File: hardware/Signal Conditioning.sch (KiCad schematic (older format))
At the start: 15 parts, among them U2 LM2902N

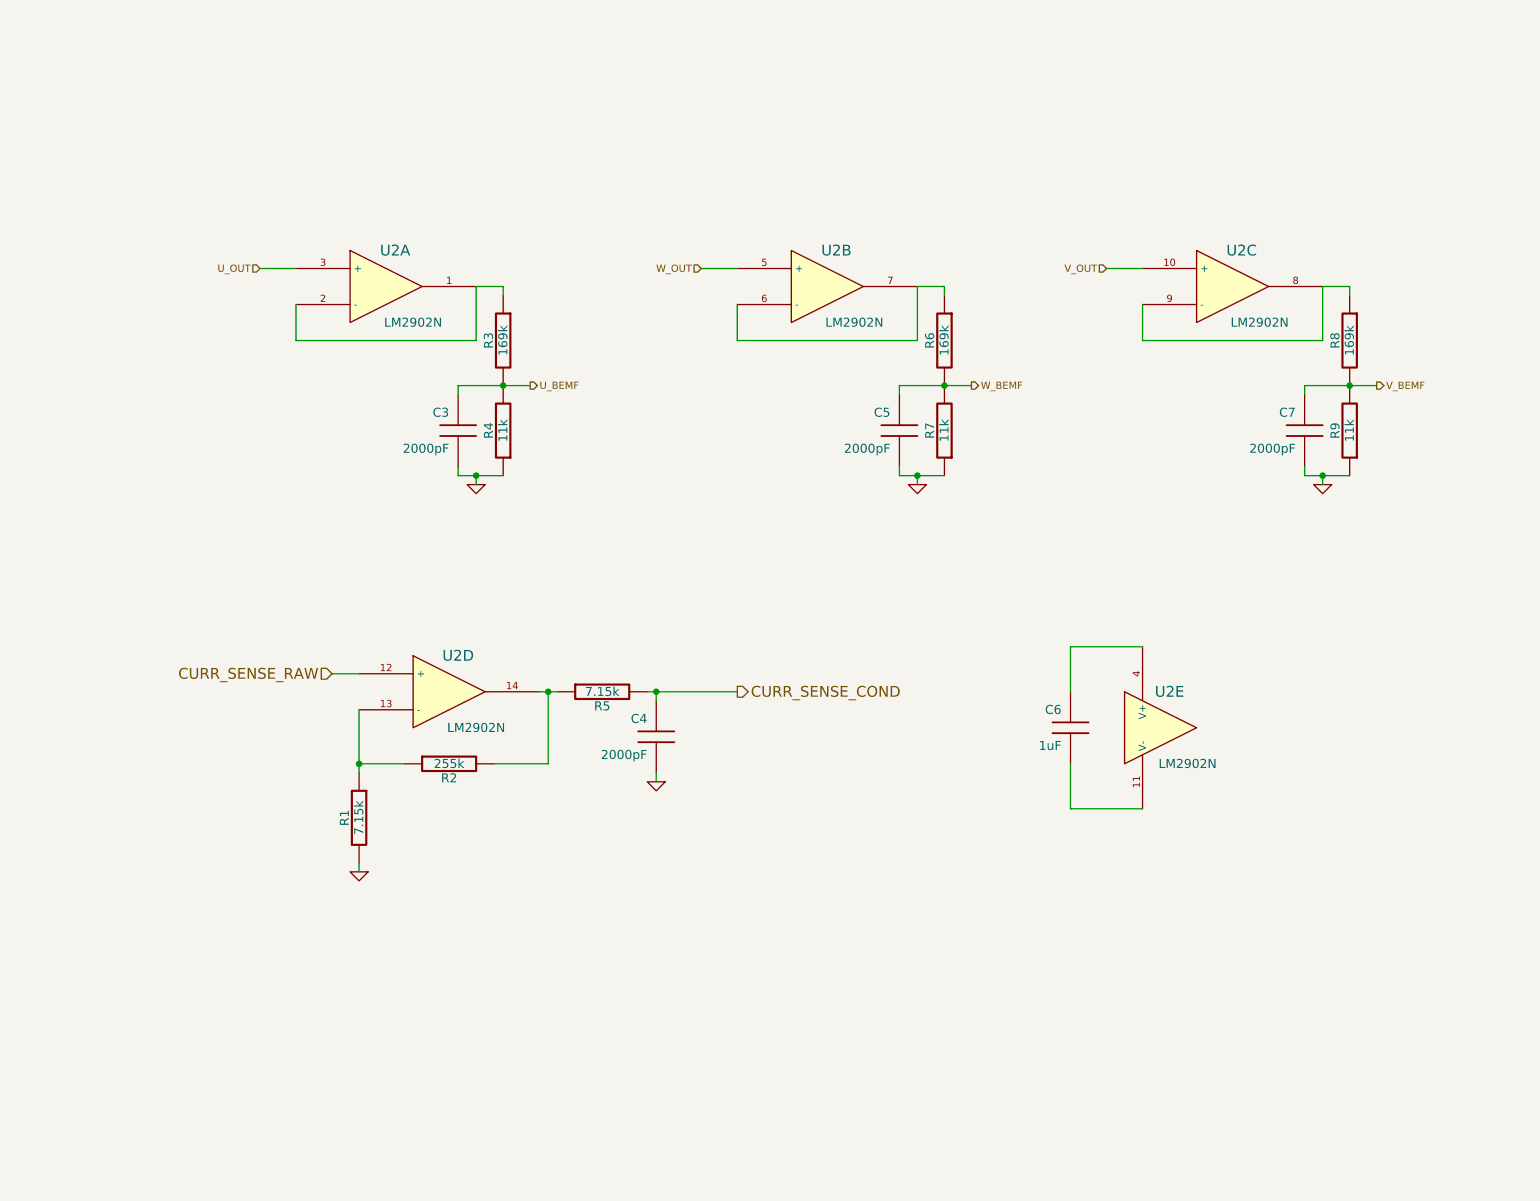
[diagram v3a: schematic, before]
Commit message: Changed the current sense conditioning to work with shunt resistor value change
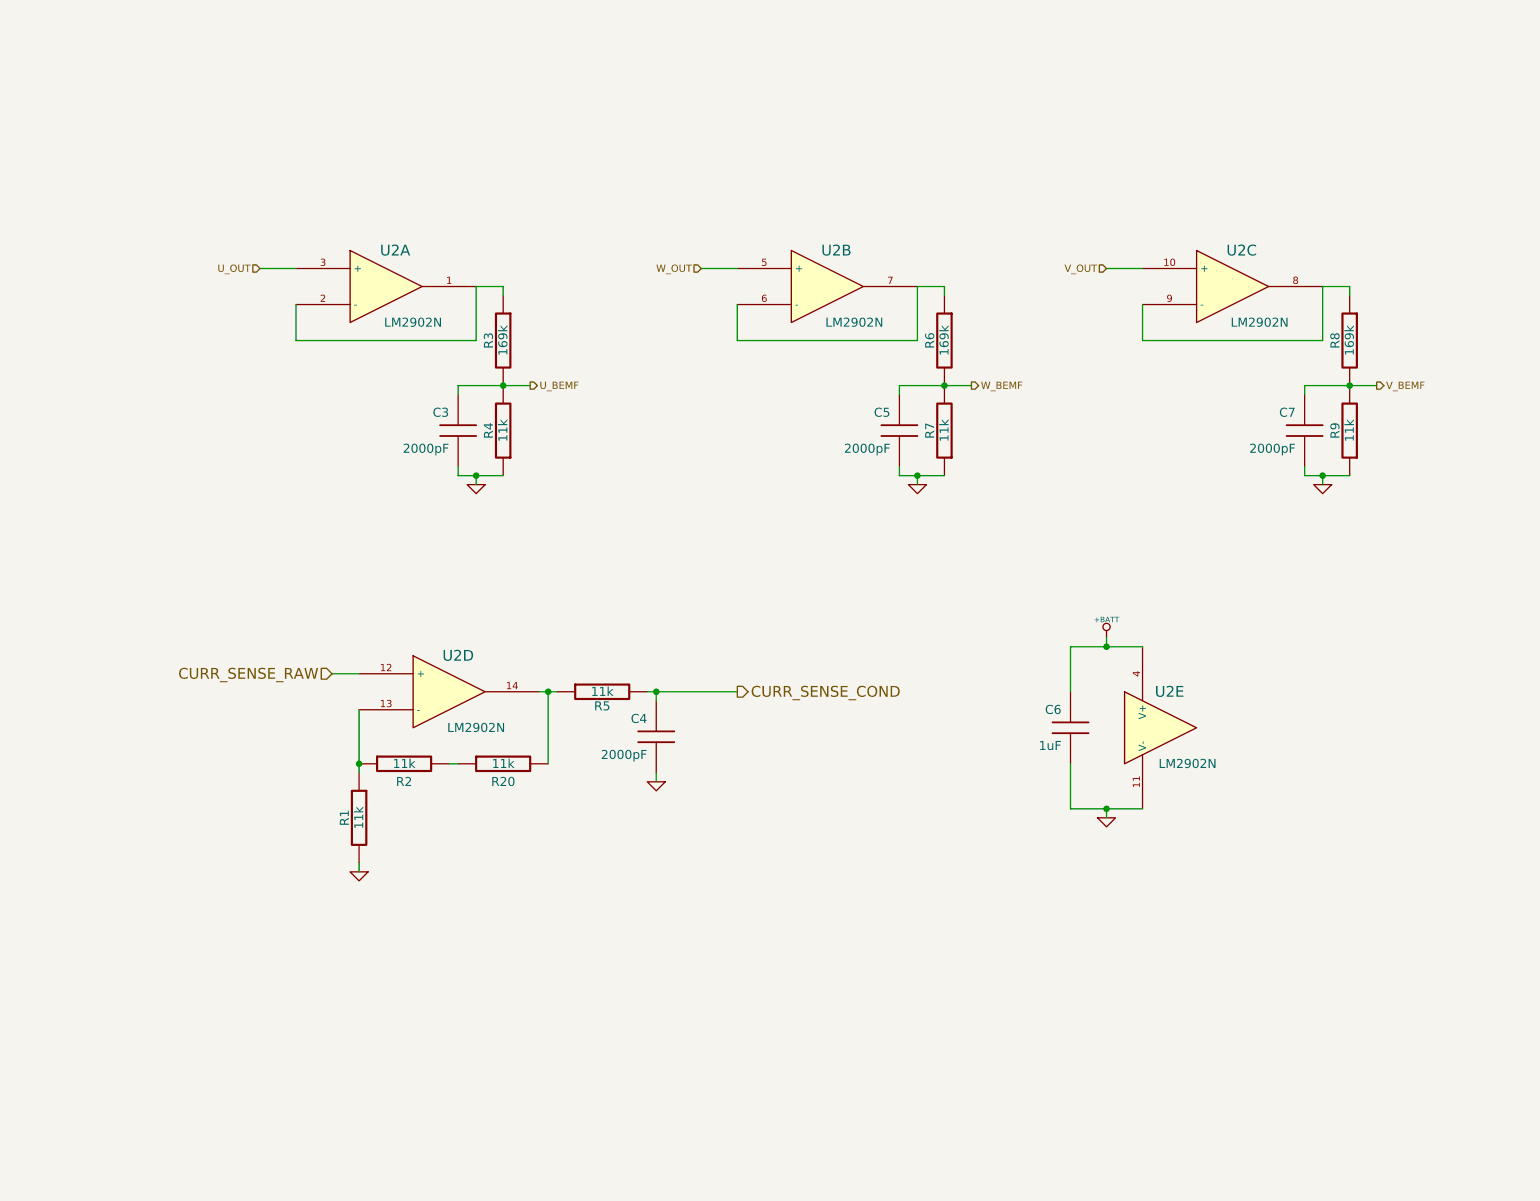
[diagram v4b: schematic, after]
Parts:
- added R20: 11k, symbol R
- R1, R5: value 7.15k -> 11k
- R2: value 255k -> 11k; Digikey P/N 255KXBK-ND -> 169KXBK-ND; Mfg P/N MFR-25FBF52-255K -> MFR-25FBF52-169K; Mouser P/N 603-MFR-25FBF52-255K -> 603-MFR-25FBF52-169K
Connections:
- net GND: now also C6.2, U2.11 (V-)
- net at R5.1, U2.14: now also R20.2; no longer R2.2
- net +BATT: now reaches C6.1, U2.4 (V+)
- new net: R2.2, R20.1
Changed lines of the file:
@@
-EESchema Schematic File Version 2  date Wed 20 May 2015 21:37:10 MST
+EESchema Schematic File Version 2  date Wed 20 May 2015 21:52:57 MST
 LIBS:power
 LIBS:device
@@
 Comment4 ""
 $EndDescr
+Wire Wire Line
+	3550 4950 3500 4950
+Connection ~ 7150 5200
+Wire Wire Line
+	7150 5250 7150 5200
+Wire Wire Line
+	4650 4550 4650 4600
+Connection ~ 4050 4550
+Wire Wire Line
+	4100 4550 4000 4550
+Wire Wire Line
+	4050 4950 4050 4550
+Connection ~ 3000 4950
+Wire Wire Line
+	3000 5000 3000 4650
+Wire Wire Line
+	6950 4950 6950 5200
+Wire Wire Line
+	6950 5200 7350 5200
+Wire Wire Line
+	4900 2200 5100 2200
+Wire Wire Line
+	7150 2200 7350 2200
+Wire Wire Line
+	2650 2200 2450 2200
+Wire Wire Line
+	6250 2350 6250 2300
+Wire Wire Line
+	3800 2350 3800 2300
+Connection ~ 6250 2850
+Wire Wire Line
+	6400 2850 6000 2850
+Connection ~ 6100 3350
+Wire Wire Line
+	6250 3350 6000 3350
+Connection ~ 8500 2850
+Wire Wire Line
+	8650 2850 8250 2850
+Connection ~ 8350 3350
+Wire Wire Line
+	8500 3350 8250 3350
+Connection ~ 3800 2850
+Wire Wire Line
+	3950 2850 3550 2850
+Connection ~ 3650 3350
+Wire Wire Line
+	3800 3350 3550 3350
+Wire Wire Line
+	3650 3400 3650 3350
+Wire Wire Line
+	3800 2300 3650 2300
+Wire Wire Line
+	8500 2300 8350 2300
+Wire Wire Line
+	8350 3400 8350 3350
+Wire Wire Line
+	6100 3400 6100 3350
+Wire Wire Line
+	6250 2300 6100 2300
+Wire Wire Line
+	3550 3350 3550 3300
+Wire Wire Line
+	3550 2850 3550 2900
+Wire Wire Line
+	8250 3350 8250 3300
+Wire Wire Line
+	8250 2850 8250 2900
+Wire Wire Line
+	6000 3350 6000 3300
+Wire Wire Line
+	6000 2850 6000 2900
+Wire Wire Line
+	3000 4450 2850 4450
+Wire Wire Line
+	8500 2300 8500 2350
+Wire Wire Line
+	2650 2400 2650 2600
+Wire Wire Line
+	2650 2600 3650 2600
+Wire Wire Line
+	3650 2600 3650 2300
+Wire Wire Line
+	7350 2400 7350 2600
+Wire Wire Line
+	7350 2600 8350 2600
+Wire Wire Line
+	8350 2600 8350 2300
+Wire Wire Line
+	5100 2400 5100 2600
+Wire Wire Line
+	5100 2600 6100 2600
+Wire Wire Line
+	6100 2600 6100 2300
+Wire Wire Line
+	6950 4550 6950 4300
+Wire Wire Line
+	6950 4300 7350 4300
+Wire Wire Line
+	3000 5500 3000 5550
+Wire Wire Line
+	4650 5000 4650 5050
+Wire Wire Line
+	5100 4550 4600 4550
+Connection ~ 4650 4550
+Wire Wire Line
+	7150 4250 7150 4300
+Connection ~ 7150 4300
+$Comp
+L R R2
+U 1 1 555D645C
+P 3250 4950
+F 0 "R2" V 3350 4950 50  0000 C CNN
+F 1 "11k" V 3250 4950 50  0000 C CNN
+F 4 "MFR-25FBF52-169K" V 3250 4950 60  0001 C CNN "Mfg P/N"
+F 5 "169KXBK-ND" V 3250 4950 60  0001 C CNN "Digikey P/N"
+F 6 "603-MFR-25FBF52-169K" V 3250 4950 60  0001 C CNN "Mouser P/N"
+	1    3250 4950
+	0    -1   1    0
+$EndComp
+$Comp
+L R R20
+U 1 1 555D6392
+P 3800 4950
+F 0 "R20" V 3900 4950 50  0000 C CNN
+F 1 "11k" V 3800 4950 50  0000 C CNN
+F 4 "MFR-25FBF52-169K" V 3800 4950 60  0001 C CNN "Mfg P/N"
+F 5 "169KXBK-ND" V 3800 4950 60  0001 C CNN "Digikey P/N"
+F 6 "603-MFR-25FBF52-169K" V 3800 4950 60  0001 C CNN "Mouser P/N"
+	1    3800 4950
+	0    -1   1    0
+$EndComp
+$Comp
+L +BATT #PWR08
+U 1 1 555D62EA
+P 7150 4250
+F 0 "#PWR08" H 7150 4200 20  0001 C CNN
+F 1 "+BATT" H 7150 4350 30  0000 C CNN
+	1    7150 4250
+	1    0    0    -1
+$EndComp
+$Comp
+L GND #PWR09
+U 1 1 555D62D6
+P 7150 5250
+F 0 "#PWR09" H 7150 5250 30  0001 C CNN
+F 1 "GND" H 7150 5180 30  0001 C CNN
+	1    7150 5250
+	1    0    0    -1
+$EndComp
 $Comp
 L R R1
@@
 P 3000 5250
 F 0 "R1" V 3080 5250 50  0000 C CNN
-F 1 "7.15k" V 3000 5250 50  0000 C CNN
+F 1 "11k" V 3000 5250 50  0000 C CNN
 F 4 "MFR-25FBF52-7K15" V 3000 5250 60  0001 C CNN "Mfg P/N"
 F 5 "7.15KXBK-ND" V 3000 5250 60  0001 C CNN "Digikey P/N"
@@
 	-1   0    0    -1
 $EndComp
-Connection ~ 4650 4550
-Wire Wire Line
-	5100 4550 4600 4550
-Wire Wire Line
-	4650 5000 4650 5050
-Wire Wire Line
-	3000 5500 3000 5550
-Wire Wire Line
-	3000 4950 3250 4950
-Wire Wire Line
-	7350 4300 6950 4300
-Wire Wire Line
-	6950 4300 6950 4550
-Wire Wire Line
-	6100 2600 6100 2300
-Wire Wire Line
-	6100 2600 5100 2600
-Wire Wire Line
-	5100 2600 5100 2400
-Wire Wire Line
-	8350 2600 8350 2300
-Wire Wire Line
-	8350 2600 7350 2600
-Wire Wire Line
-	7350 2600 7350 2400
-Wire Wire Line
-	3650 2600 3650 2300
-Wire Wire Line
-	3650 2600 2650 2600
-Wire Wire Line
-	2650 2600 2650 2400
-Wire Wire Line
-	8500 2350 8500 2300
-Wire Wire Line
-	3000 4450 2850 4450
-Wire Wire Line
-	6000 2900 6000 2850
-Wire Wire Line
-	6000 3300 6000 3350
-Wire Wire Line
-	8250 2900 8250 2850
-Wire Wire Line
-	8250 3300 8250 3350
-Wire Wire Line
-	3550 2900 3550 2850
-Wire Wire Line
-	3550 3300 3550 3350
-Wire Wire Line
-	6100 2300 6250 2300
-Wire Wire Line
-	6100 3400 6100 3350
-Wire Wire Line
-	8350 3400 8350 3350
-Wire Wire Line
-	8500 2300 8350 2300
-Wire Wire Line
-	3650 2300 3800 2300
-Wire Wire Line
-	3650 3400 3650 3350
-Wire Wire Line
-	3550 3350 3800 3350
-Connection ~ 3650 3350
-Wire Wire Line
-	3550 2850 3950 2850
-Connection ~ 3800 2850
-Wire Wire Line
-	8250 3350 8500 3350
-Connection ~ 8350 3350
-Wire Wire Line
-	8250 2850 8650 2850
-Connection ~ 8500 2850
-Wire Wire Line
-	6000 3350 6250 3350
-Connection ~ 6100 3350
-Wire Wire Line
-	6000 2850 6400 2850
-Connection ~ 6250 2850
-Wire Wire Line
-	3800 2300 3800 2350
-Wire Wire Line
-	6250 2300 6250 2350
-Wire Wire Line
-	2650 2200 2450 2200
-Wire Wire Line
-	7150 2200 7350 2200
-Wire Wire Line
-	4900 2200 5100 2200
-Wire Wire Line
-	7350 5200 6950 5200
-Wire Wire Line
-	6950 5200 6950 4950
-Wire Wire Line
-	3000 5000 3000 4650
-Connection ~ 3000 4950
-Wire Wire Line
-	3750 4950 4050 4950
-Wire Wire Line
-	4050 4950 4050 4550
-Wire Wire Line
-	4100 4550 4000 4550
-Connection ~ 4050 4550
-Wire Wire Line
-	4650 4550 4650 4600
-$Comp
-L GND #PWR08
+$Comp
+L GND #PWR010
 U 1 1 554659C8
 P 4650 5050
-F 0 "#PWR08" H 4650 5050 30  0001 C CNN
+F 0 "#PWR010" H 4650 5050 30  0001 C CNN
 F 1 "GND" H 4650 4980 30  0001 C CNN
 	1    4650 5050
@@
 P 4350 4550
 F 0 "R5" V 4430 4550 50  0000 C CNN
-F 1 "7.15k" V 4350 4550 50  0000 C CNN
+F 1 "11k" V 4350 4550 50  0000 C CNN
 F 4 "MFR-25FBF52-7K15" V 4350 4550 60  0001 C CNN "Mfg P/N"
 F 5 "7.15KXBK-ND" V 4350 4550 60  0001 C CNN "Digikey P/N"
@@
 $EndComp
 $Comp
-L GND #PWR09
+L GND #PWR011
 U 1 1 5546596B
 P 3000 5550
-F 0 "#PWR09" H 3000 5550 30  0001 C CNN
+F 0 "#PWR011" H 3000 5550 30  0001 C CNN
 F 1 "GND" H 3000 5480 30  0001 C CNN
 	1    3000 5550
 	-1   0    0    -1
-$EndComp
-$Comp
-L R R2
-U 1 1 5546592D
-P 3500 4950
-F 0 "R2" V 3580 4950 50  0000 C CNN
-F 1 "255k" V 3500 4950 50  0000 C CNN
-F 4 "MFR-25FBF52-255K" V 3500 4950 60  0001 C CNN "Mfg P/N"
-F 5 "255KXBK-ND" V 3500 4950 60  0001 C CNN "Digikey P/N"
-F 6 "603-MFR-25FBF52-255K" V 3500 4950 60  0001 C CNN "Mouser P/N"
-	1    3500 4950
-	0    -1   1    0
 $EndComp
 $Comp
@@
 $EndComp
 $Comp
-L GND #PWR010
+L GND #PWR012
 U 1 1 5533F7C4
 P 3650 3400
-F 0 "#PWR010" H 3650 3400 30  0001 C CNN
+F 0 "#PWR012" H 3650 3400 30  0001 C CNN
 F 1 "GND" H 3650 3330 30  0001 C CNN
 	1    3650 3400
@@
 $EndComp
 $Comp
-L GND #PWR011
+L GND #PWR013
 U 1 1 5533F7C3
 P 8350 3400
-F 0 "#PWR011" H 8350 3400 30  0001 C CNN
+F 0 "#PWR013" H 8350 3400 30  0001 C CNN
 F 1 "GND" H 8350 3330 30  0001 C CNN
 	1    8350 3400
@@
 $EndComp
 $Comp
-L GND #PWR012
+L GND #PWR014
 U 1 1 5533F7BA
 P 6100 3400
-F 0 "#PWR012" H 6100 3400 30  0001 C CNN
+F 0 "#PWR014" H 6100 3400 30  0001 C CNN
 F 1 "GND" H 6100 3330 30  0001 C CNN
 	1    6100 3400
